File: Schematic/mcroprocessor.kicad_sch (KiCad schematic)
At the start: 11 parts, among them SW1 SW_Push, U1 STM32F091RCT6

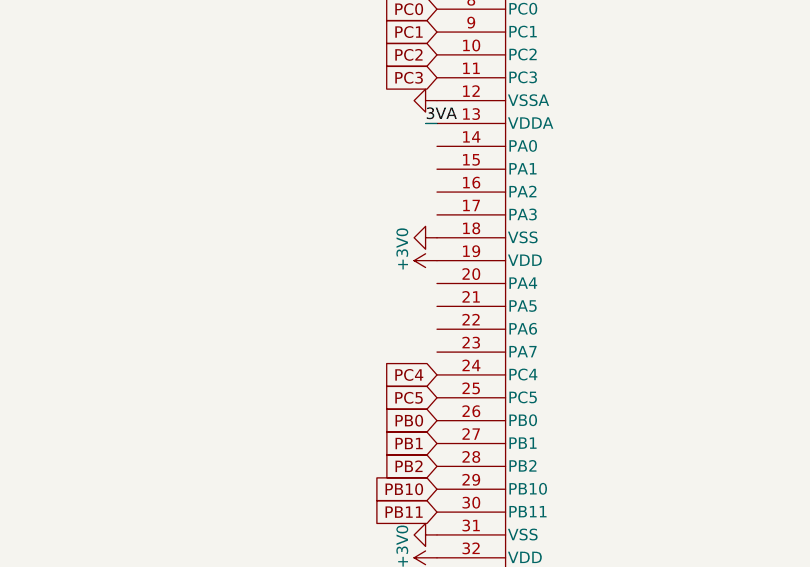
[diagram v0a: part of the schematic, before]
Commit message: Added audio circuitry
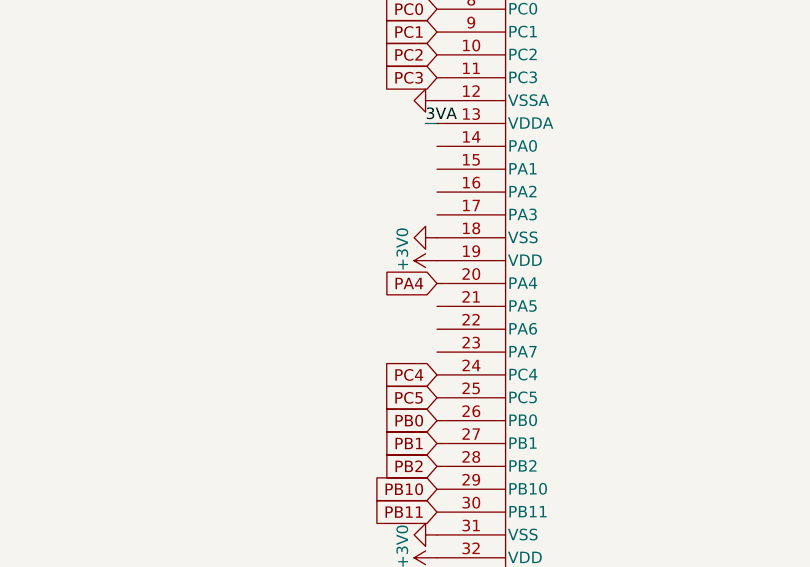
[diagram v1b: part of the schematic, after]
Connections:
- net PA4: now reaches U1.20 (PA4)
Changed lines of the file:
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@@
+    )
+  )
+  (global_label "PA4" (shape input) (at 78.74 85.09 180) (fields_autoplaced)
+    (effects (font (size 1.27 1.27)) (justify right))
+    (property "Intersheetrefs" "${INTERSHEET_REFS}" (at 72.2661 85.09 0)
+      (effects (font (size 1.27 1.27)) (justify right) hide)
     )
   )

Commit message: initial CB design
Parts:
- added J3: Conn_02x05_Odd_Even, Connector_IDC:IDC-Header_2x05_P2.54mm_Vertical, symbol Connector_Generic:Conn_02x05_Odd_Even
- added LD1: LED_Red, LED_THT:LED_D5.0mm, symbol stm32f091-rescue:LED_Small_ALT-Device
- added R1: 5.1k, Resistor_SMD:R_1206_3216Metric_Pad1.30x1.75mm_HandSolder, symbol Device:R_US
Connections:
- net GND: now also J3.3 (Pin_3), J3.4 (Pin_4), LD1.1 (K); no longer C9.2, U1.12 (VSSA)
- net NRST: now also J3.1 (Pin_1)
- net 3VA renamed VA
- net PC14 renamed SWDIO_IN
- net SWDIO_IN: now also J3.2 (Pin_2)
- net PC15 renamed SWCLK_IN
- net SWCLK_IN: now also J3.6 (Pin_6)
- new net: LD1.2 (A), R1.2
- new net GNDA: C9.2, U1.12 (VSSA)
- new net U5V: J3.10 (Pin_10), J3.9 (Pin_9), R1.1
- no-connect marks 0 -> 3
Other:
- note added: "1.8V @ 0.7mA"
- moved on the sheet: C11, C5, C6, C7, C8, C9, FB1, R10, R3, SW1

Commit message: Most of the schematic and PCB layout.
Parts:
- R1: value 5.1k -> 10k
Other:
- note removed: "1.8V @ 0.7mA"
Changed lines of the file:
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@@
-    (effects (font (size 1.27 1.27)) (justify left bottom))
-  )
-  (text "1.8V @ 0.7mA" (at 203.2 102.87 0)
     (effects (font (size 1.27 1.27)) (justify left bottom))
   )
@@
       (effects (font (size 1.27 1.27)) (justify left))
     )
-    (property "Value" "5.1k" (at 221.4372 96.393 0)
+    (property "Value" "10k" (at 221.4372 96.393 0)
       (effects (font (size 1.27 1.27)) (justify left))
     )

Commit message: Added stuff from today
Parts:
- added J3: Conn_01x03_Pin, Connector_PinSocket_2.54mm:PinSocket_1x03_P2.54mm_Vertical, symbol Connector:Conn_01x03_Pin
- added LD1: LED_Red, LED_THT:LED_D5.0mm, symbol stm32f091-rescue:LED_Small_ALT-Device
- added R1: 5.6k, Resistor_SMD:R_1206_3216Metric_Pad1.30x1.75mm_HandSolder, symbol Device:R_US
- added U6: MAX7375AXR805, Package_TO_SOT_SMD:SOT-323_SC-70, symbol Oscillator:MAX7375AXR805
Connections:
- net +3V0: now also U6.1 (V+)
- net GND: now also LD1.1 (K), U6.3 (GND)
- net SWCLK_IN: now also U1.45 (PA12); no longer U1.4 (PC15-OSC32_OUT)
- net SWDIO_IN: now also U1.46 (PA13); no longer U1.3 (PC14-OSC32_IN)
- net PA0: now reaches U1.14 (PA0)
- net PA0: now also J3.1 (Pin_1)
- net PA1: now reaches U1.15 (PA1)
- net PA1: now also J3.2 (Pin_2)
- net PA2: now reaches U1.16 (PA2)
- net PA2: now also J3.3 (Pin_3)
- net PA3: now reaches U1.17 (PA3)
- net at U1.21 (PA5): now also R1.1
- new net: U1.3 (PC14-OSC32_IN), U6.2 (CLOCK)
- new net: LD1.2 (A), R1.2

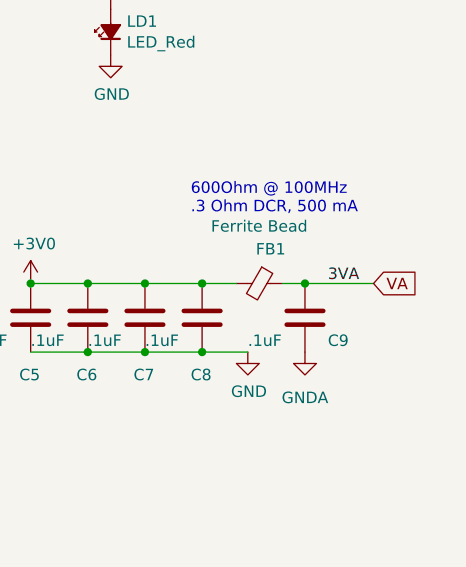
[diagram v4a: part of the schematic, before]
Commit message: Added sensors. Fixed other stuff.
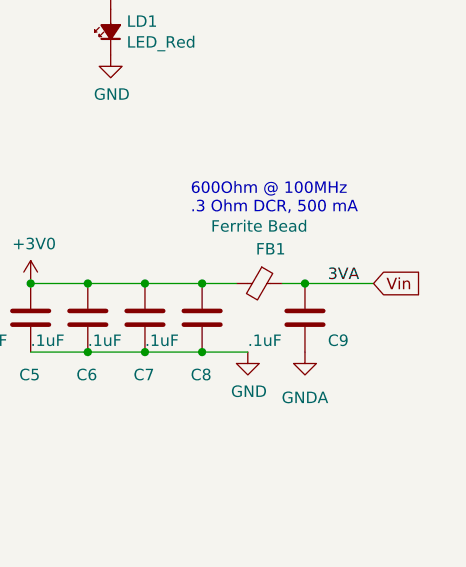
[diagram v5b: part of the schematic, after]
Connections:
- net VA renamed Vin
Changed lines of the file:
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@@
     )
   )
-  (global_label "VA" (shape input) (at 248.92 129.54 0) (fields_autoplaced)
+  (global_label "Vin" (shape input) (at 248.92 129.54 0) (fields_autoplaced)
     (effects (font (size 1.27 1.27)) (justify left))
-    (property "Intersheetrefs" "${INTERSHEET_REFS}" (at 254.003 129.54 0)
+    (property "Intersheetrefs" "${INTERSHEET_REFS}" (at 254.6682 129.54 0)
       (effects (font (size 1.27 1.27)) (justify left) hide)
     )

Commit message: Mostly finallized PCB
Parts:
- J3: value Conn_02x05_Odd_Even -> DEBUG_HEADER
- SW1: value SW_Push -> RESET
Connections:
- net SWCLK_IN: now also U1.49 (PA14); no longer U1.45 (PA12)
- net at U6.2 (CLOCK): now also U1.5 (PF0-OSC_IN); no longer U1.3 (PC14-OSC32_IN)
- net PA7: now reaches U1.23 (PA7)

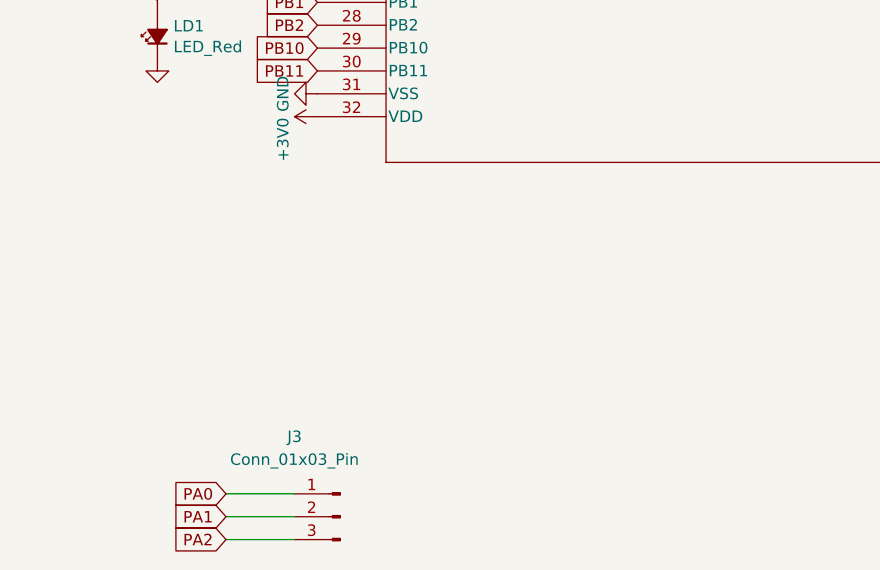
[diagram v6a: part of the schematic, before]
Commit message: Added images
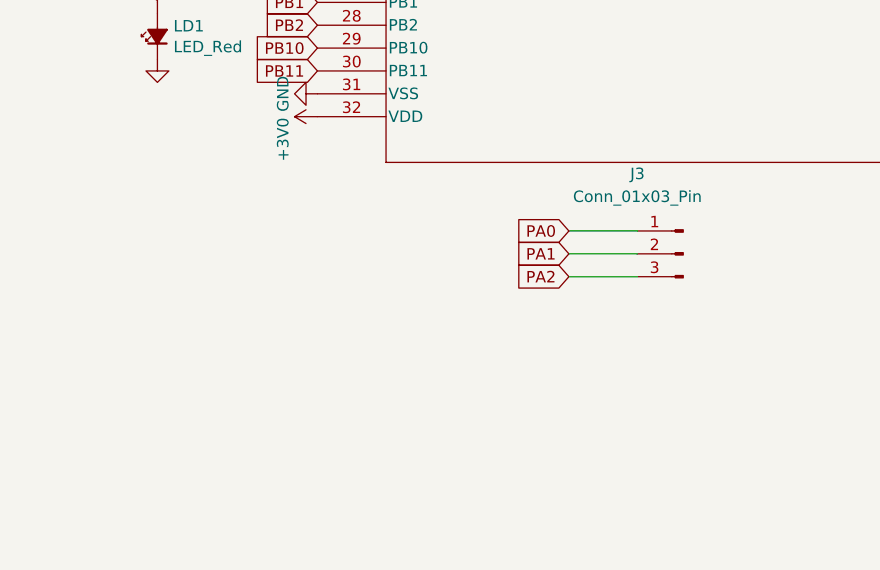
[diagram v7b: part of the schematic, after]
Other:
- moved on the sheet: J3
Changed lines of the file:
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@@
     (stroke (width 0) (type default))
   )
-  (wire (pts (xy 68.58 162.56) (xy 76.2 162.56))
+  (wire (pts (xy 106.68 133.35) (xy 114.3 133.35))
     (stroke (width 0) (type default))
   )
@@
     (stroke (width 0) (type default))
   )
-  (wire (pts (xy 68.58 160.02) (xy 76.2 160.02))
+  (wire (pts (xy 106.68 130.81) (xy 114.3 130.81))
     (stroke (width 0) (type default))
   )
@@
     (stroke (width 0) (type default))
   )
-  (wire (pts (xy 68.58 157.48) (xy 76.2 157.48))
+  (wire (pts (xy 106.68 128.27) (xy 114.3 128.27))
     (stroke (width 0) (type default))
   )
@@
     )
   )
-  (global_label "PA0" (shape input) (at 68.58 157.48 180) (fields_autoplaced)
-    (effects (font (size 1.27 1.27)) (justify right))
-    (property "Intersheetrefs" "${INTERSHEET_REFS}" (at 62.1061 157.48 0)
+  (global_label "PA0" (shape input) (at 106.68 128.27 180) (fields_autoplaced)
+    (effects (font (size 1.27 1.27)) (justify right))
+    (property "Intersheetrefs" "${INTERSHEET_REFS}" (at 100.2061 128.27 0)
       (effects (font (size 1.27 1.27)) (justify right) hide)
     )
@@
     )
   )
-  (global_label "PA2" (shape input) (at 68.58 162.56 180) (fields_autoplaced)
-    (effects (font (size 1.27 1.27)) (justify right))
-    (property "Intersheetrefs" "${INTERSHEET_REFS}" (at 62.1061 162.56 0)
+  (global_label "PA2" (shape input) (at 106.68 133.35 180) (fields_autoplaced)
+    (effects (font (size 1.27 1.27)) (justify right))
+    (property "Intersheetrefs" "${INTERSHEET_REFS}" (at 100.2061 133.35 0)
       (effects (font (size 1.27 1.27)) (justify right) hide)
     )
@@
     )
   )
-  (global_label "PA1" (shape input) (at 68.58 160.02 180) (fields_autoplaced)
-    (effects (font (size 1.27 1.27)) (justify right))
-    (property "Intersheetrefs" "${INTERSHEET_REFS}" (at 62.1061 160.02 0)
+  (global_label "PA1" (shape input) (at 106.68 130.81 180) (fields_autoplaced)
+    (effects (font (size 1.27 1.27)) (justify right))
+    (property "Intersheetrefs" "${INTERSHEET_REFS}" (at 100.2061 130.81 0)
       (effects (font (size 1.27 1.27)) (justify right) hide)
     )
@@
     )
   )
-  (symbol (lib_id "Connector:Conn_01x03_Pin") (at 81.28 160.02 0) (mirror y) (unit 1)
-    (in_bom yes) (on_board yes) (dnp no)
-    (property "Reference" "J3" (at 76.2 151.13 0)
-      (effects (font (size 1.27 1.27)))
-    )
-    (property "Value" "Conn_01x03_Pin" (at 76.2 153.67 0)
-      (effects (font (size 1.27 1.27)))
-    )
-    (property "Footprint" "Connector_PinSocket_2.54mm:PinSocket_1x03_P2.54mm_Vertical" (at 81.28 160.02 0)
-      (effects (font (size 1.27 1.27)) hide)
-    )
-    (property "Datasheet" "~" (at 81.28 160.02 0)
-      (effects (font (size 1.27 1.27)) hide)
-    )
+  (symbol (lib_id "Connector:Conn_01x03_Pin") (at 119.38 130.81 0) (mirror y) (unit 1)
+    (in_bom yes) (on_board yes) (dnp no)
+    (property "Reference" "J3" (at 114.3 121.92 0)
+      (effects (font (size 1.27 1.27)))
+    )
+    (property "Value" "Conn_01x03_Pin" (at 114.3 124.46 0)
+      (effects (font (size 1.27 1.27)))
+    )
+    (property "Footprint" "Connector_PinSocket_2.54mm:PinSocket_1x03_P2.54mm_Vertical" (at 119.38 130.81 0)
+      (effects (font (size 1.27 1.27)) hide)
+    )
+    (property "Datasheet" "~" (at 119.38 130.81 0)
+      (effects (font (size 1.27 1.27)) hide)
+    )

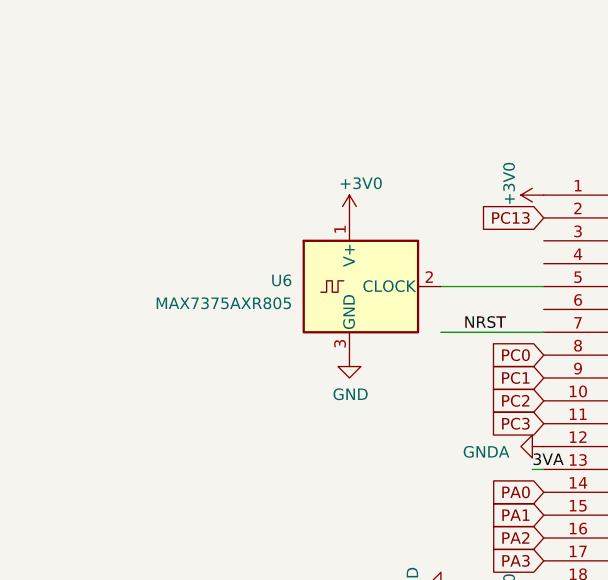
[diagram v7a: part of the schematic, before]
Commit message: Added Cap to osilator, and fixed posible issues with signals near it.
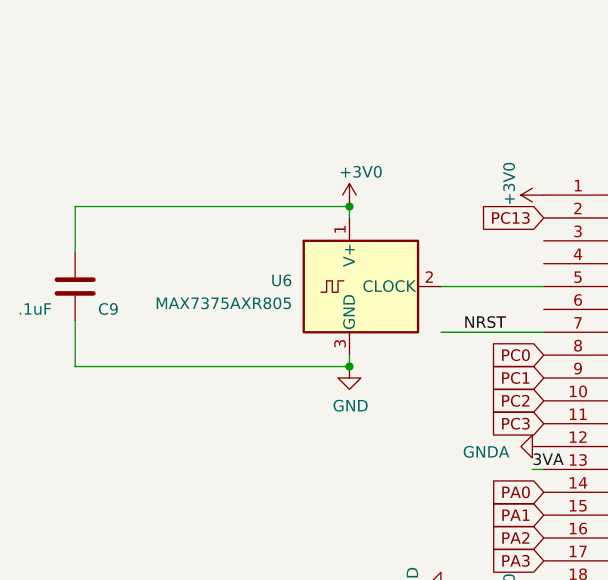
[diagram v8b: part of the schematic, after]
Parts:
- added C9: .1uF, Capacitor_SMD:C_0805_2012Metric_Pad1.18x1.45mm_HandSolder, symbol Device:C
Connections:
- net +3V0: now also C9.1
- net GND: now also C9.2
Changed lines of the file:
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@@
   (junction (at 228.6 31.75) (diameter 0) (color 0 0 0 0)
+  )
+  (junction (at 57.15 55.88) (diameter 0) (color 0 0 0 0)
+  )
+  (junction (at 57.15 38.1) (diameter 0) (color 0 0 0 0)
   )
   (junction (at 219.71 83.82) (diameter 0) (color 0 0 0 0)
@@
     (stroke (width 0) (type default))
   )
+  (wire (pts (xy 57.15 55.88) (xy 57.15 54.61))
+    (stroke (width 0) (type default))
+  )
   (wire (pts (xy 219.71 83.82) (xy 219.71 91.44))
     (stroke (width 0) (type default))
@@
     (stroke (width 0) (type default))
   )
+  (wire (pts (xy 26.67 55.88) (xy 26.67 50.8))
+    (stroke (width 0) (type default))
+  )
   (wire (pts (xy 222.25 71.12) (xy 210.82 71.12))
     (stroke (width 0) (type default))
@@
     (stroke (width 0) (type default))
   )
+  (wire (pts (xy 57.15 38.1) (xy 57.15 39.37))
+    (stroke (width 0) (type default))
+  )
   (wire (pts (xy 210.82 129.54) (xy 217.17 129.54))
     (stroke (width 0) (type default))
@@
     (stroke (width 0) (type default))
   )
+  (wire (pts (xy 57.15 55.88) (xy 26.67 55.88))
+    (stroke (width 0) (type default))
+  )
   (wire (pts (xy 68.58 80.01) (xy 78.74 80.01))
     (stroke (width 0) (type default))
@@
     (stroke (width 0) (type default))
   )
+  (wire (pts (xy 26.67 43.18) (xy 26.67 38.1))
+    (stroke (width 0) (type default))
+  )
   (wire (pts (xy 154.94 82.55) (xy 162.56 82.55))
     (stroke (width 0) (type default))
   )
   (wire (pts (xy 78.74 87.63) (xy 60.96 87.63))
+    (stroke (width 0) (type default))
+  )
+  (wire (pts (xy 26.67 38.1) (xy 57.15 38.1))
     (stroke (width 0) (type default))
   )
@@
     )
   )
-  (symbol (lib_id "power:GND") (at 57.15 54.61 0) (unit 1)
-    (in_bom yes) (on_board yes) (dnp no)
-    (property "Reference" "#PWR0130" (at 57.15 60.96 0)
-      (effects (font (size 1.27 1.27)) hide)
-    )
-    (property "Value" "GND" (at 57.277 59.0042 0)
-      (effects (font (size 1.27 1.27)))
-    )
-    (property "Footprint" "" (at 57.15 54.61 0)
-      (effects (font (size 1.27 1.27)) hide)
-    )
-    (property "Datasheet" "" (at 57.15 54.61 0)
+  (symbol (lib_id "power:GND") (at 57.15 55.88 0) (unit 1)
+    (in_bom yes) (on_board yes) (dnp no)
+    (property "Reference" "#PWR0130" (at 57.15 62.23 0)
+      (effects (font (size 1.27 1.27)) hide)
+    )
+    (property "Value" "GND" (at 57.277 60.2742 0)
+      (effects (font (size 1.27 1.27)))
+    )
+    (property "Footprint" "" (at 57.15 55.88 0)
+      (effects (font (size 1.27 1.27)) hide)
+    )
+    (property "Datasheet" "" (at 57.15 55.88 0)
       (effects (font (size 1.27 1.27)) hide)
     )
@@
     )
   )
+  (symbol (lib_id "Device:C") (at 26.67 46.99 0) (unit 1)
+    (in_bom yes) (on_board yes) (dnp no)
+    (property "Reference" "C9" (at 29.21 49.53 0)
+      (effects (font (size 1.27 1.27)) (justify left))
+    )
+    (property "Value" ".1uF" (at 20.32 49.53 0)
+      (effects (font (size 1.27 1.27)) (justify left))
+    )
+    (property "Footprint" "Capacitor_SMD:C_0805_2012Metric_Pad1.18x1.45mm_HandSolder" (at 27.6352 50.8 0)
+      (effects (font (size 1.27 1.27)) hide)
+    )
+    (property "Datasheet" "" (at 26.67 46.99 0)
+      (effects (font (size 1.27 1.27)) hide)
+    )
+    (pin "1")
+    (pin "2")
+    (instances
+      (project "stm32f091"
+        (path "/1a854c3f-f20e-4271-9c06-678b7140bb2e"
+          (reference "C9") (unit 1)
+        )
+      )
+      (project "Schematic"
+        (path "/ced54cd9-3b34-40e4-aa66-964aaab81b0a/49528601-a054-44d2-8cd6-b055d7d9a1ef"
+          (reference "C16") (unit 1)
+        )
+      )
+    )
+  )
   (symbol (lib_id "power:+3V0") (at 78.74 115.57 90) (unit 1)
     (in_bom yes) (on_board yes) (dnp no)
@@
     )
   )
-  (symbol (lib_id "power:+3V0") (at 57.15 39.37 0) (unit 1)
-    (in_bom yes) (on_board yes) (dnp no)
-    (property "Reference" "#PWR0105" (at 57.15 43.18 0)
-      (effects (font (size 1.27 1.27)) hide)
-    )
-    (property "Value" "+3V0" (at 58.42 35.56 0)
-      (effects (font (size 1.27 1.27)))
-    )
-    (property "Footprint" "" (at 57.15 39.37 0)
-      (effects (font (size 1.27 1.27)) hide)
-    )
-    (property "Datasheet" "" (at 57.15 39.37 0)
-      (effects (font (size 1.27 1.27)) hide)
-    )
+  (symbol (lib_id "power:+3V0") (at 57.15 38.1 0) (unit 1)
+    (in_bom yes) (on_board yes) (dnp no)
+    (property "Reference" "#PWR0105" (at 57.15 41.91 0)
+      (effects (font (size 1.27 1.27)) hide)
+    )
+    (property "Value" "+3V0" (at 58.42 34.29 0)
+      (effects (font (size 1.27 1.27)))
+    )
+    (property "Footprint" "" (at 57.15 38.1 0)
+      (effects (font (size 1.27 1.27)) hide)
+    )
+    (property "Datasheet" "" (at 57.15 38.1 0)
+      (effects (font (size 1.27 1.27)) hide)
+    )
